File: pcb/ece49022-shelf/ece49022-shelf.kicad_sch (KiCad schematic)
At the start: 5 parts, among them J2 Conn_01x16_Pin, J3 Conn_01x04_Pin, J5 Conn_01x02_Pin, J6 Conn_01x02_Pin

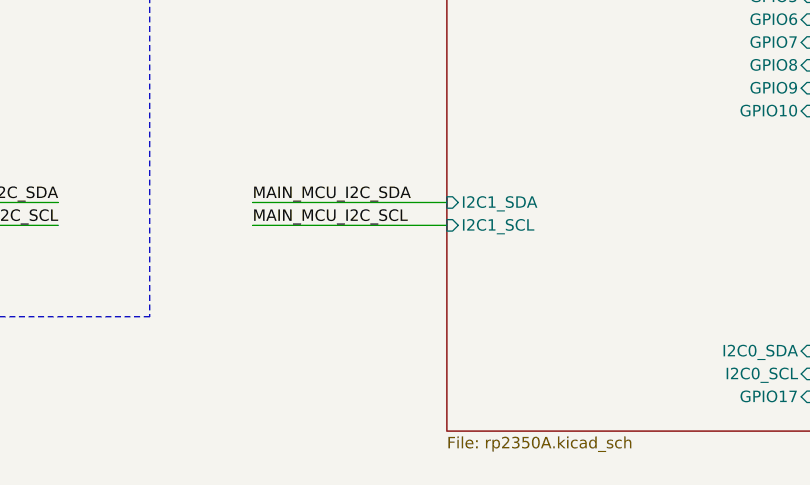
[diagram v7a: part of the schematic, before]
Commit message: edited shelf power and added power for interface PCB
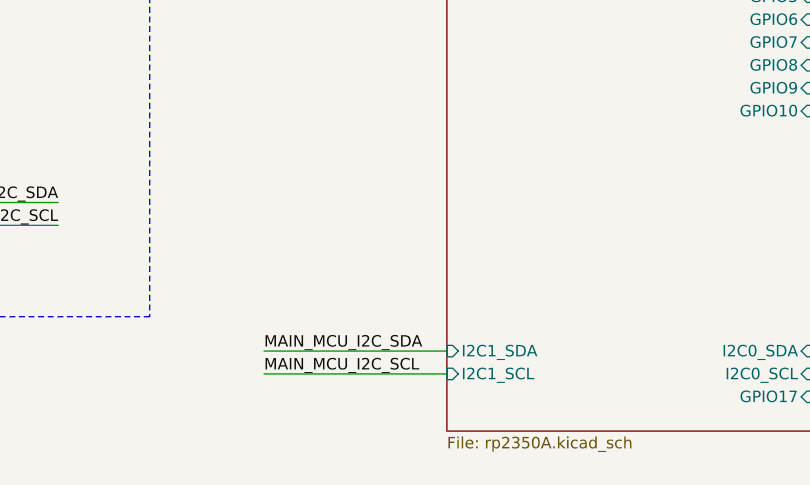
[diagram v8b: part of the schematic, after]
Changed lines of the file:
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@@
 	(wire
 		(pts
-			(xy 73.66 115.57) (xy 95.25 115.57)
+			(xy 74.93 132.08) (xy 95.25 132.08)
 		)
 		(stroke
@@
 	(wire
 		(pts
-			(xy 73.66 113.03) (xy 95.25 113.03)
+			(xy 74.93 129.54) (xy 95.25 129.54)
 		)
 		(stroke
@@
 	)
 	(label "MAIN_MCU_I2C_SCL"
-		(at 73.66 115.57 0)
+		(at 74.93 132.08 0)
 		(effects
 			(font
@@
 	)
 	(label "MAIN_MCU_I2C_SDA"
-		(at 73.66 113.03 0)
+		(at 74.93 129.54 0)
 		(effects
 			(font
@@
 		)
 		(pin "I2C1_SDA" input
-			(at 95.25 113.03 180)
+			(at 95.25 129.54 180)
 			(effects
 				(font
@@
 		)
 		(pin "I2C1_SCL" input
-			(at 95.25 115.57 180)
-			(effects
-				(font
+			(at 95.25 132.08 180)
+			(effects
+				(font
